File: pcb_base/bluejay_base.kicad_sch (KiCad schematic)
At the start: 9 parts

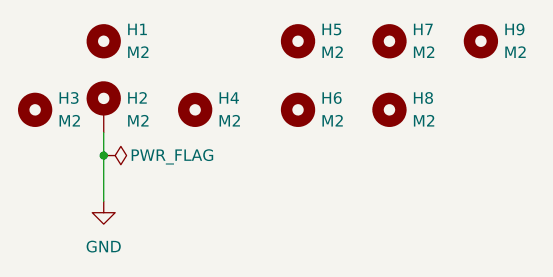
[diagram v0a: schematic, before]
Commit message: Update schematics in preparation for review
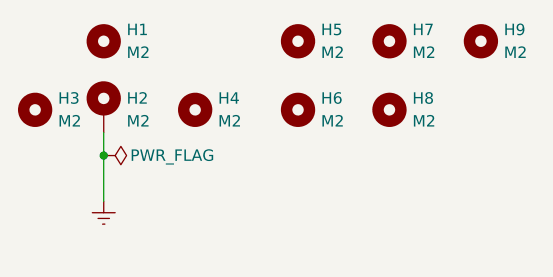
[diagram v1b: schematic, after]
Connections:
- net GND renamed Earth
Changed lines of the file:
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@@
   (title_block
     (title "BlueJay Base")
+    (rev "1.0")
   )
   (junction (at 120.65 113.03) (diameter 0) (color 0 0 0 0)
@@
     )
   )
-  (symbol (lib_id "power:GND") (at 120.65 118.11 0) (unit 1)
+  (symbol (lib_id "power:Earth") (at 120.65 118.11 0) (unit 1)
     (in_bom yes) (on_board yes) (fields_autoplaced)
     (property "Reference" "#PWR0115" (id 0) (at 120.65 124.46 0)
       (effects (font (size 1.27 1.27)) hide)
     )
-    (property "Value" "GND" (id 1) (at 120.65 123.19 0))
+    (property "Value" "Earth" (id 1) (at 120.65 121.92 0)
+      (effects (font (size 1.27 1.27)) hide)
+    )
     (property "Footprint" "" (id 2) (at 120.65 118.11 0)
       (effects (font (size 1.27 1.27)) hide)
     )
-    (property "Datasheet" "" (id 3) (at 120.65 118.11 0)
+    (property "Datasheet" "~" (id 3) (at 120.65 118.11 0)
       (effects (font (size 1.27 1.27)) hide)
     )
@@
     )
     (path "/aa799aa4-0b77-4e69-bd3a-b95b04823f1a"
-      (reference "#PWR0115") (unit 1) (value "GND") (footprint "")
+      (reference "#PWR0115") (unit 1) (value "Earth") (footprint "")
     )
     (path "/d0420dde-bff1-4dd4-b50e-a8ff439a9375"

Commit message: Fine tuning of schematics and pcbs in prep for review
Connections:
- net Earth renamed GND
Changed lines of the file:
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@@
     )
   )
-  (symbol (lib_id "power:Earth") (at 120.65 118.11 0) (unit 1)
+  (symbol (lib_id "power:GND") (at 120.65 118.11 0) (unit 1)
     (in_bom yes) (on_board yes) (fields_autoplaced)
     (property "Reference" "#PWR0115" (id 0) (at 120.65 124.46 0)
       (effects (font (size 1.27 1.27)) hide)
     )
-    (property "Value" "Earth" (id 1) (at 120.65 121.92 0)
-      (effects (font (size 1.27 1.27)) hide)
-    )
+    (property "Value" "GND" (id 1) (at 120.65 121.92 0))
     (property "Footprint" "" (id 2) (at 120.65 118.11 0)
       (effects (font (size 1.27 1.27)) hide)
@@
     )
     (path "/aa799aa4-0b77-4e69-bd3a-b95b04823f1a"
-      (reference "#PWR0115") (unit 1) (value "Earth") (footprint "")
+      (reference "#PWR0115") (unit 1) (value "GND") (footprint "")
     )
     (path "/d0420dde-bff1-4dd4-b50e-a8ff439a9375"

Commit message: remove mounting hole 9
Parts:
- removed H9: M2, MountingHole:MountingHole_2.2mm_M2_Pad, symbol Mechanical:MountingHole
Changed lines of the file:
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@@
     (pin "1")
-  )
-  (symbol (lib_id "Mechanical:MountingHole") (at 162.56 100.33 0) (unit 1)
-    (in_bom no) (on_board yes) (fields_autoplaced)
-    (property "Reference" "H9" (id 0) (at 165.1 99.0599 0)
-      (effects (font (size 1.27 1.27)) (justify left))
-    )
-    (property "Value" "M2" (id 1) (at 165.1 101.5999 0)
-      (effects (font (size 1.27 1.27)) (justify left))
-    )
-    (property "Footprint" "MountingHole:MountingHole_2.2mm_M2_Pad" (id 2) (at 162.56 100.33 0)
-      (effects (font (size 1.27 1.27)) hide)
-    )
-    (property "Datasheet" "~" (id 3) (at 162.56 100.33 0)
-      (effects (font (size 1.27 1.27)) hide)
-    )
   )
   (symbol (lib_id "Mechanical:MountingHole") (at 152.4 100.33 0) (unit 1)
@@
       (reference "H8") (unit 1) (value "M2") (footprint "MountingHole:MountingHole_2.2mm_M2_Pad")
     )
-    (path "/88babb1f-a86c-44c4-9ecd-f3e8d1f4aef4"
-      (reference "H9") (unit 1) (value "M2") (footprint "MountingHole:MountingHole_2.2mm_M2_Pad")
-    )
   )

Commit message: Update placement of some components and size of drill holes
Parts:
- removed H7, H8: M2, MountingHole:MountingHole_2.2mm_M2_Pad, symbol Mechanical:MountingHole
- renumbered H3 to H2, H2 to H3
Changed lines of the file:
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@@
   (symbol (lib_id "Mechanical:MountingHole_Pad") (at 120.65 107.95 0) (unit 1)
     (in_bom yes) (on_board yes) (fields_autoplaced)
-    (property "Reference" "H2" (id 0) (at 123.19 106.6799 0)
+    (property "Reference" "H3" (id 0) (at 123.19 106.6799 0)
       (effects (font (size 1.27 1.27)) (justify left))
     )
@@
   (symbol (lib_name "MountingHole_1") (lib_id "Mechanical:MountingHole") (at 113.03 107.95 0) (unit 1)
     (in_bom yes) (on_board yes) (fields_autoplaced)
-    (property "Reference" "H3" (id 0) (at 115.57 106.6799 0)
+    (property "Reference" "H2" (id 0) (at 115.57 106.6799 0)
       (effects (font (size 1.27 1.27)) (justify left))
     )
@@
     )
     (pin "1")
-  )
-  (symbol (lib_id "Mechanical:MountingHole") (at 152.4 100.33 0) (unit 1)
-    (in_bom no) (on_board yes) (fields_autoplaced)
-    (property "Reference" "H7" (id 0) (at 154.94 99.0599 0)
-      (effects (font (size 1.27 1.27)) (justify left))
-    )
-    (property "Value" "M2" (id 1) (at 154.94 101.5999 0)
-      (effects (font (size 1.27 1.27)) (justify left))
-    )
-    (property "Footprint" "MountingHole:MountingHole_2.2mm_M2_Pad" (id 2) (at 152.4 100.33 0)
-      (effects (font (size 1.27 1.27)) hide)
-    )
-    (property "Datasheet" "~" (id 3) (at 152.4 100.33 0)
-      (effects (font (size 1.27 1.27)) hide)
-    )
-  )
-  (symbol (lib_id "Mechanical:MountingHole") (at 152.4 107.95 0) (unit 1)
-    (in_bom no) (on_board yes) (fields_autoplaced)
-    (property "Reference" "H8" (id 0) (at 154.94 106.6799 0)
-      (effects (font (size 1.27 1.27)) (justify left))
-    )
-    (property "Value" "M2" (id 1) (at 154.94 109.2199 0)
-      (effects (font (size 1.27 1.27)) (justify left))
-    )
-    (property "Footprint" "MountingHole:MountingHole_2.2mm_M2_Pad" (id 2) (at 152.4 107.95 0)
-      (effects (font (size 1.27 1.27)) hide)
-    )
-    (property "Datasheet" "~" (id 3) (at 152.4 107.95 0)
-      (effects (font (size 1.27 1.27)) hide)
-    )
   )
   (symbol (lib_id "power:GND") (at 120.65 118.11 0) (unit 1)
@@
       (reference "H1") (unit 1) (value "M2") (footprint "MountingHole:MountingHole_2.2mm_M2_Pad")
     )
-    (path "/4a35a674-388c-438a-8da0-ee33b6fc37e8"
+    (path "/552b5d1f-a593-40c3-a973-202071f3c188"
       (reference "H2") (unit 1) (value "M2") (footprint "MountingHole:MountingHole_2.2mm_M2_Pad")
     )
-    (path "/552b5d1f-a593-40c3-a973-202071f3c188"
+    (path "/4a35a674-388c-438a-8da0-ee33b6fc37e8"
       (reference "H3") (unit 1) (value "M2") (footprint "MountingHole:MountingHole_2.2mm_M2_Pad")
     )
@@
       (reference "H6") (unit 1) (value "M2") (footprint "MountingHole:MountingHole_2.2mm_M2_Pad")
     )
-    (path "/8ff55002-cb98-4e23-b57e-209cc7ec712a"
-      (reference "H7") (unit 1) (value "M2") (footprint "MountingHole:MountingHole_2.2mm_M2_Pad")
-    )
-    (path "/a73aae4f-b04b-4d16-8b11-ca3d57da8772"
-      (reference "H8") (unit 1) (value "M2") (footprint "MountingHole:MountingHole_2.2mm_M2_Pad")
-    )
   )
